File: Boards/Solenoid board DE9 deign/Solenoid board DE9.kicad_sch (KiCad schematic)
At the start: 2 parts, among them J2 DE9_Receptacle_MountingHoles

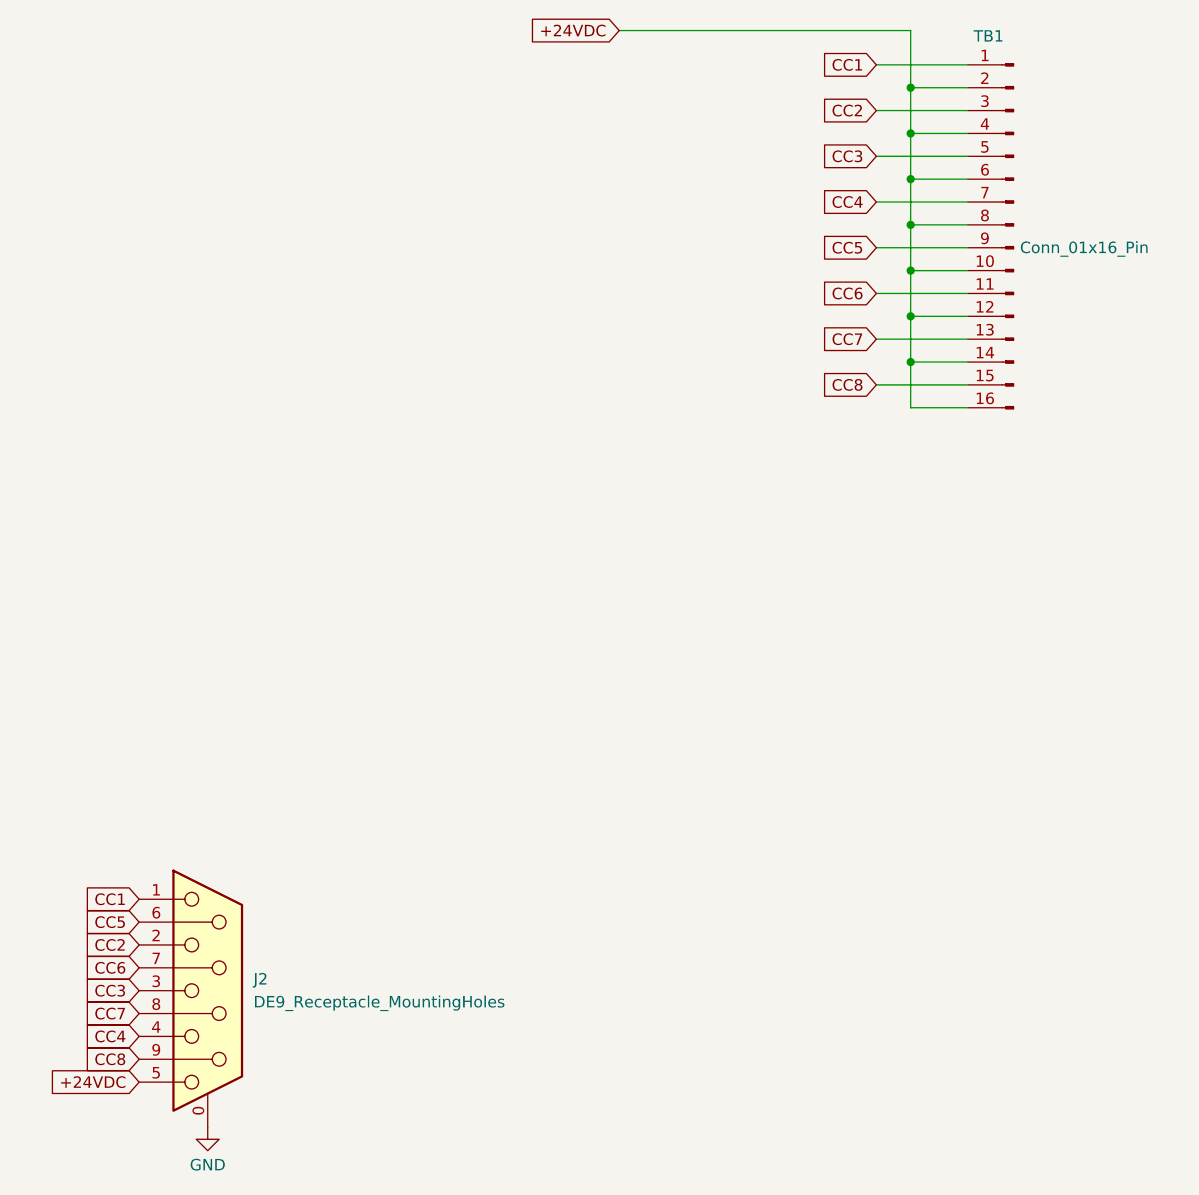
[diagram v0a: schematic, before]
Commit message: added audio board schematics and de9 board fab files
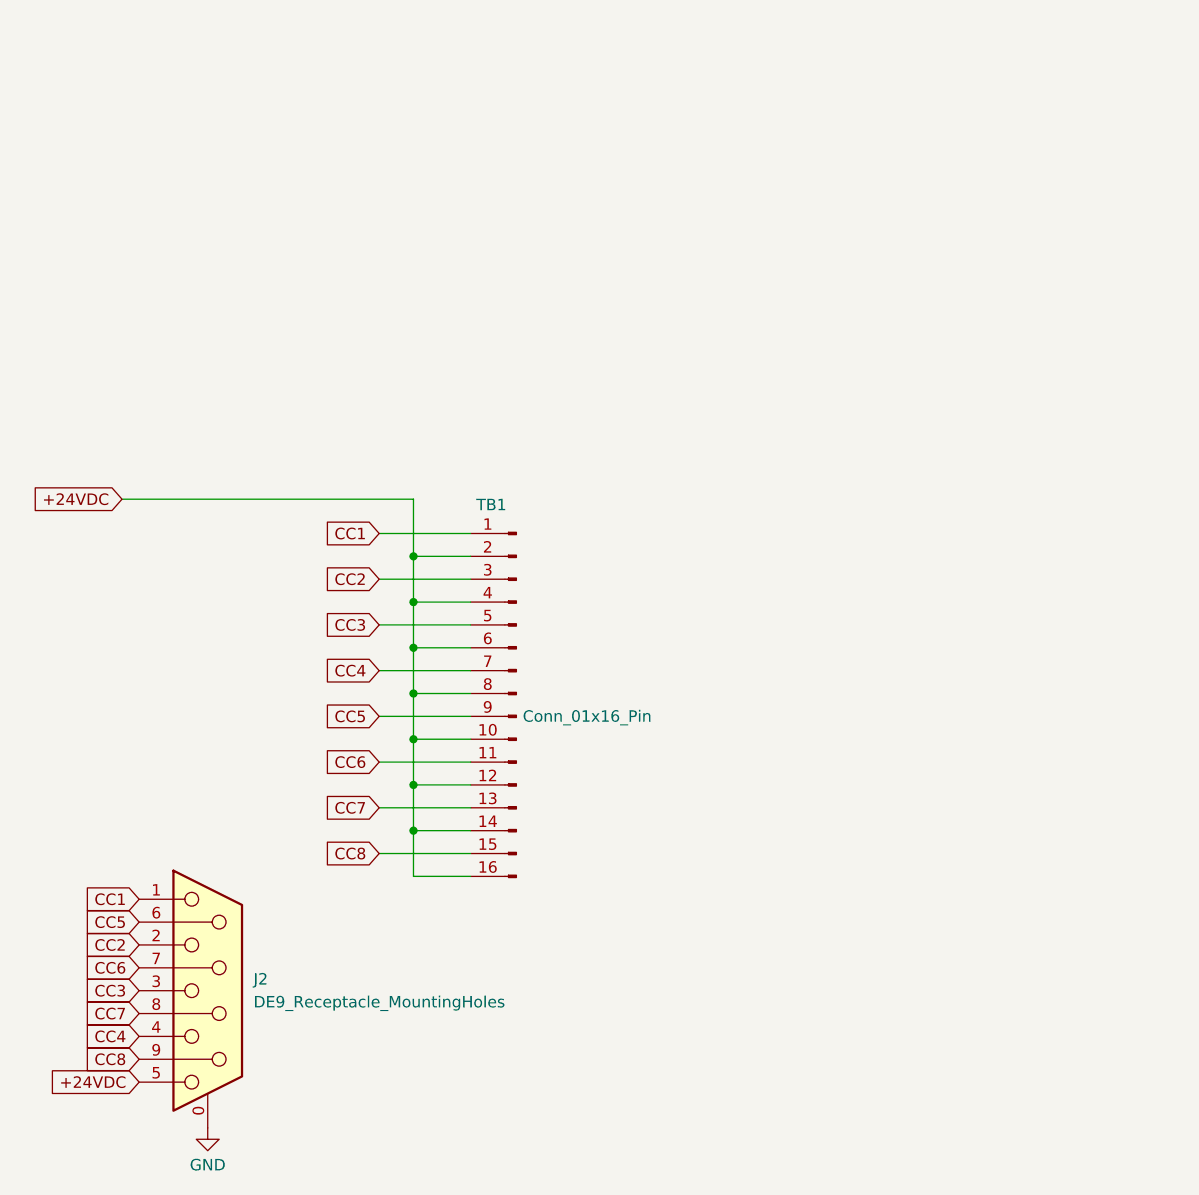
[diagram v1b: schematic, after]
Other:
- moved on the sheet: TB1
